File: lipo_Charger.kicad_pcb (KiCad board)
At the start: 4 copper layers, 81.4 x 80.8 mm, 111 parts, among them J1 XT60PW-M, J2 Conn_01x01, J3 balance_plug_4s, J4 Conn_01x05, J5 Conn_01x04, J6 Conn_01x01, J7 Conn_01x07, J8 Conn_01x04, Q1 NX7002AK_215(nch low power), Q2 NVTFS010N10MCLTAG(high power)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

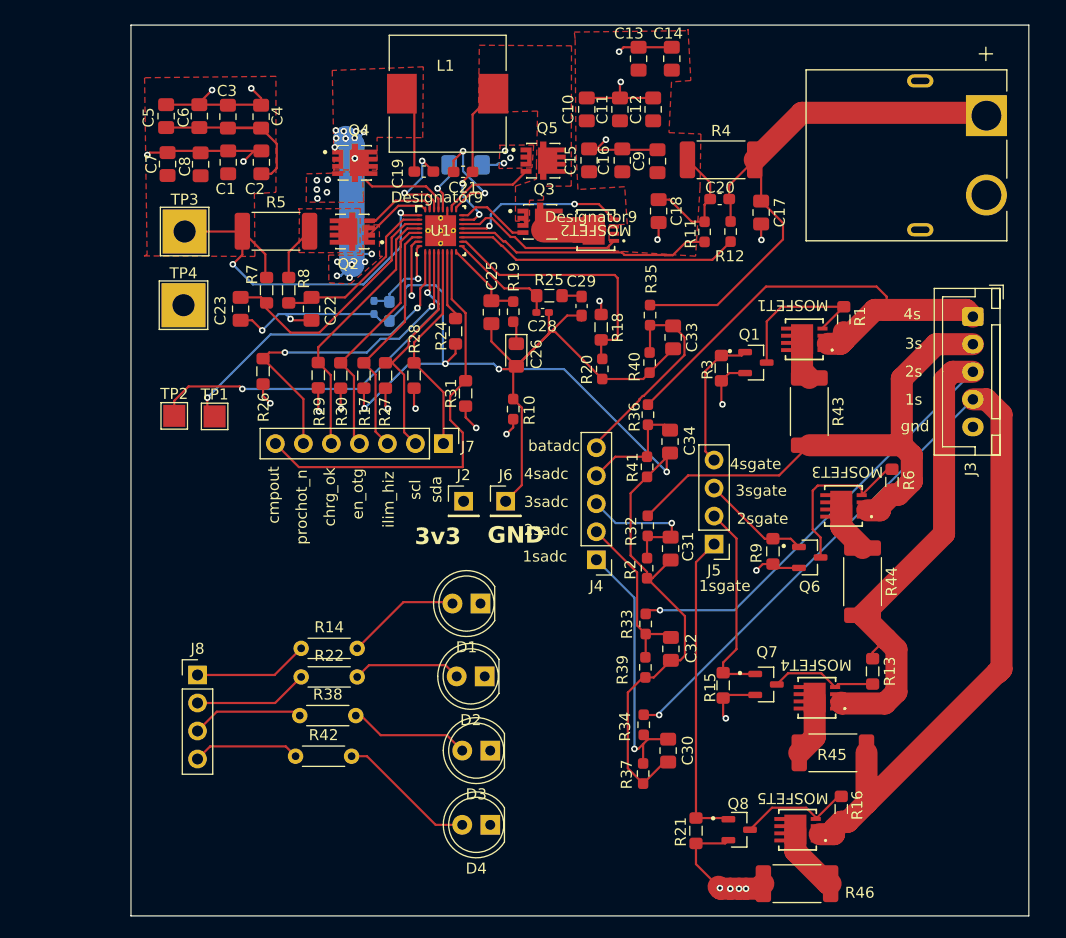
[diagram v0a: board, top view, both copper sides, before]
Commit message: xt60 conenector was in the wrong direction now resolved all the footprints has been verfied by cross checking the components bought balance plug not yet got in hand that has to be checcked
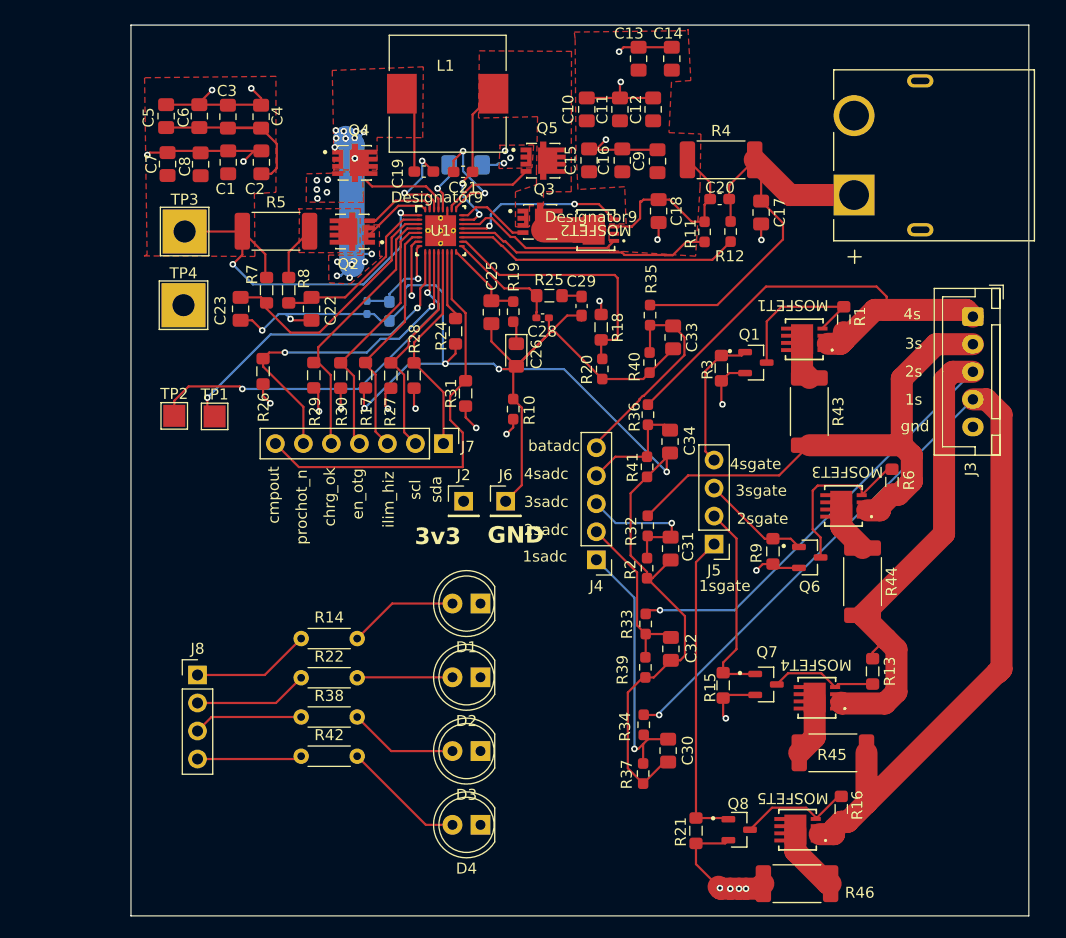
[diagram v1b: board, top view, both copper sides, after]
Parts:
- moved R14 0.89 mm to (111.4, 109.6)
- moved D3 0.89 mm to (127.6, 119.8)
- moved D4 0.88 mm to (127.6, 126.5)
- moved R23 0.64 mm to (117.3, 79.6)
- moved R42 0.51 mm to (111.4, 120.3)
- moved C28 0.48 mm to (133.3, 80.5)
- moved R27 0.48 mm to (119.5, 85.8)
- moved R29 0.41 mm to (112.5, 85.7)
- moved D2 0.39 mm to (127.6, 113.1)
- moved R38 0.18 mm to (111.4, 116.7)
- moved R17 0.15 mm to (117.2, 85.7)
- moved R22 0.08 mm to (111.4, 113.2)
- turned J1 to 90 degrees
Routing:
- net /BAT: track 52.6 -> 40.1 mm
- net /VSYS: track 27.5 -> 33.4 mm
- net Net-(D4-A): track 12.6 -> 11.2 mm
- net Net-(D2-A): track 9.88 -> 8.66 mm
- net Net-(D3-A): track 11.0 -> 9.92 mm
- net Net-(U1-IADPT): track 8.43 -> 9.06 mm
- net /CHRG_OK: track 24.4 -> 25.0 mm

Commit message: copper pour mismatch due to some glitches rectified it no erc error
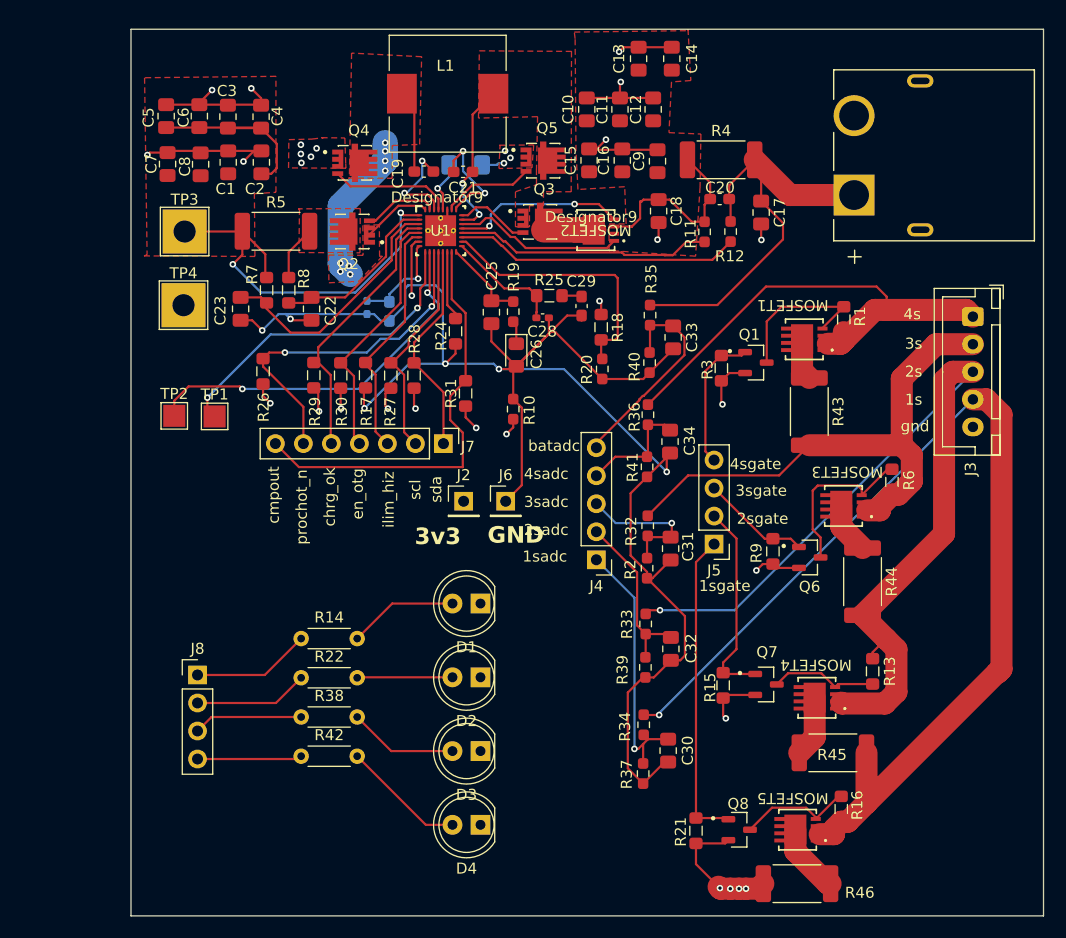
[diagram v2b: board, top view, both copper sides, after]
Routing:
- net /copper_pour2: track 37.9 -> 27.8 mm, vias 15 -> 8
- net Net-(U1-LODRV1): track 8.28 -> 11.1 mm
- net +24V: track 53.5 -> 54.1 mm
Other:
- board size 81.4 x 80.8 mm -> 82.7 x 80.4 mm

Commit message: final correction has been ready to order
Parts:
- removed D3, D4: LED, LED_THT:LED_D5.0mm
- removed J8: Conn_01x04, Connector_PinHeader_2.54mm:PinHeader_1x04_P2.54mm_Vertical
- removed R38, R42: R, Resistor_THT:R_Axial_DIN0204_L3.6mm_D1.6mm_P5.08mm_Horizontal
- added J10: Conn_01x20, Connector_PinHeader_2.54mm:PinHeader_1x20_P2.54mm_Vertical, F.Cu at (90.0, 130.4)
- added J11: Conn_01x20, Connector_PinHeader_2.54mm:PinHeader_1x20_P2.54mm_Vertical, F.Cu at (90.0, 126.6)
- added J12: Conn_01x20, Connector_PinHeader_2.54mm:PinHeader_1x20_P2.54mm_Vertical, F.Cu at (90.0, 111.4)
- added J13: Conn_01x02, Connector_PinHeader_2.54mm:PinHeader_1x02_P2.54mm_Vertical, F.Cu at (90.0, 103.1)
- added J9: Conn_01x20, Connector_PinHeader_2.54mm:PinHeader_1x20_P2.54mm_Vertical, F.Cu at (90.0, 107.1)
- moved D1 41.2 mm to (90.8, 87.9), turned to -90 degrees
- moved D2 33.8 mm to (99.2, 94.9)
- moved R14 24.8 mm to (89.0, 98.8), turned to 90 degrees
- moved R22 21.5 mm to (94.6, 99.7)
- moved TP1 0.43 mm to (103.1, 89.4)
- moved TP2 0.43 mm to (99.4, 89.4)
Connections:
- net /PROCHOT_N renamed /PB0
- net /SCL renamed /PB10
- net /SDA renamed /PB3
- net Net-(J5-Pin_1) renamed /1SGATE
- net Net-(J5-Pin_2) renamed /2SGATE
- net Net-(J5-Pin_3) renamed /3SGATE
- net Net-(J5-Pin_4) renamed /4SGATE
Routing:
- net GNDA: track 161.4 -> 221.8 mm, vias 6 -> 8
- net /5V: track 0.00 -> 58.5 mm
- net /4SGATE: track 12.7 -> 62.4 mm
- net /3SGATE: track 9.91 -> 54.9 mm
- net /PB3: track 19.6 -> 62.7 mm
- net /2SGATE: track 18.5 -> 59.3 mm
- net /PB10: track 20.1 -> 58.9 mm
- net /1SGATE: track 28.5 -> 65.4 mm
- net /BAT_adc: track 19.4 -> 54.5 mm
- net /CELL_4S_adc: track 10.5 -> 41.5 mm
- net /CELL_3S_adc: track 13.0 -> 38.1 mm
- net /CELL_1S_adc: track 24.3 -> 47.8 mm, vias 1 -> 2
- net /CELL_2S_adc: track 15.7 -> 38.3 mm
- net /EN_OTG: track 23.3 -> 45.4 mm
- net /ILIM_HIZ: track 21.9 -> 44.0 mm
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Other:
- board size 82.7 x 80.4 mm -> 92.1 x 80.4 mm

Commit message: final ordered file
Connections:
- J10 pad 14: /4SGATE -> /1SGATE
- J10 pad 15: /3SGATE -> /2SGATE
- J10 pad 16: /2SGATE -> /3SGATE
- J10 pad 17: /1SGATE -> /4SGATE
- J11 pad 14: /4SGATE -> /1SGATE
- J11 pad 15: /3SGATE -> /2SGATE
- J11 pad 16: /2SGATE -> /3SGATE
- J11 pad 17: /1SGATE -> /4SGATE
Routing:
- net /1SGATE: track 65.4 -> 86.6 mm
- net /2SGATE: track 59.3 -> 75.2 mm
- net /3SGATE: track 54.9 -> 66.8 mm
- net /PB3: track 62.7 -> 66.6 mm
- net /CELL_1S_adc: track 47.8 -> 44.5 mm
- net /4SGATE: track 62.4 -> 65.1 mm
- net GNDA: track 221.8 -> 223.0 mm
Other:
- board text added: "Asunama"
